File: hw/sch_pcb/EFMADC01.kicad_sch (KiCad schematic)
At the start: 36 parts, among them J1 3.3-5V, J2 HEADER_2x01, J4 HEADER_2x01_PARALLEL, J5 HEADER_2x01_PARALLEL, J6 HEADER_2x01_PARALLEL, J7 HEADER_2x01_PARALLEL, J9 MCX, M1 RFShield_TwoPieces, M2 HOLE, M3 HOLE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

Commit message: Rounted PCB Added silkscreen text.
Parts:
- removed C6: 1uF, Mlab_L:FIR_0805, symbol PCRD06A-rescue:EMI_Filter_C-Device
- removed C7: 100nF, Capacitor_SMD:C_0805_2012Metric, symbol ISM02A-rescue:C_Small-Device-ISM02A-rescue
- removed C9: 10uF, Capacitor_Tantalum_SMD:CP_EIA-3216-18_Kemet-A, symbol Device:C_Polarized
- removed D2: BZV55C-6,2V, Diode_SMD:D_MiniMELF, symbol ISM02A-rescue:D_ZENER-MLAB_D
- added C6, C7: 100nF, Capacitor_SMD:C_0805_2012Metric, symbol Device:C
- added C9: 10uF, Capacitor_SMD:C_0805_2012Metric, symbol Device:C
- added D2: BZV55C-6,2V, Diode_SMD:D_MiniMELF, symbol Device:D_Zener
- added R4, R5, R6, R7: 33R, Resistor_SMD:R_0805_2012Metric, symbol Device:R
- C1, C2, C3: footprint Capacitor_SMD:C_0603_1608Metric -> Capacitor_SMD:C_0805_2012Metric; UST_ID 5c70984812875079b91f8bf2 -> 6508260b462c6d9e720541f1
- C10, C12: UST_ID 5c70984812875079b91f8bf2 -> 5c70984712875079b91f8b4c
- C4: footprint Capacitor_SMD:C_0603_1608Metric -> Capacitor_SMD:C_0805_2012Metric; UST_ID 5c70984812875079b91f8bec -> 5c70984812875079b91f8ba6
- C5: footprint Capacitor_SMD:C_0603_1608Metric -> Capacitor_SMD:C_0805_2012Metric; UST_ID 5c70984812875079b91f8bf2 -> 5c70984712875079b91f8b4c
- D1: footprint Diode_SMD:D_SOD-523 -> Diode_SMD:D_SMB
- M1: UST_ID2 5c7275631287500b4e11302f -> (none)
- R1, R2, R3: footprint Resistor_SMD:R_0603_1608Metric -> Resistor_SMD:R_0805_2012Metric
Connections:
- net +3.3VA is gone; now on net VCC: C5.2, U1.1 (Vin), U2.5 (V+)
- net GND: now also C6.2, C9.2, D2.2 (A)
- net GNDA: now also C7.2
- net VCC: now also C8.1, J1.3, J1.4, C6.1, C7.1, C9.1, D2.1 (K)
- net at J4.1, J4.2: now also R4.2; no longer U4.8 (SCK)
- net at J7.1, J7.2: now also R7.2; no longer U4.1 (CONV)
- net at J5.1, J5.2: now also R5.2; no longer U4.7 (SDO)
- net at J6.1, J6.2: now also R6.2; no longer U4.6 (SDI)
- new net: R7.1, U4.1 (CONV)
- new net: R4.1, U4.8 (SCK)
- new net: R5.1, U4.7 (SDO)
- new net: R6.1, U4.6 (SDI)
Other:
- moved on the sheet: C1, D1, J4, J5, J6, J7, U1

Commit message: Cleanup net names in schematics.
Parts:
- U1: value ISL21080DIH312Z-TK 1V25 -> ISL21080CIH315ZT; UST_ID 5c70984712875079b91f8b7a -> 5c70984712875079b91f8b0a
- U3: UST_ID (none) -> 67d36d64ee7fc534862c3ebc
- U4: UST_ID (none) -> 651eae84462c6d9e7205573b
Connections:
- net REF_1V25 renamed REF
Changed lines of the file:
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@@
 		)
 	)
-	(label "REF_1V25"
+	(label "REF"
 		(at 91.44 106.68 180)
 		(effects
@@
 		)
 	)
-	(label "REF_1V25"
+	(label "REF"
 		(at 148.59 128.27 180)
 		(effects
@@
 		)
 	)
-	(label "REF_1V25"
+	(label "REF"
 		(at 109.22 160.02 180)
 		(effects
@@
 		)
 	)
-	(label "REF_1V25"
+	(label "REF"
 		(at 60.96 49.53 0)
 		(effects
@@
 			)
 		)
-		(property "Value" "ISL21080DIH312Z-TK  1V25"
+		(property "Value" "ISL21080CIH315ZT"
 			(at 41.91 40.64 90)
 			(effects
@@
 			)
 		)
-		(property "Description" "2.0V 25μA Micropower Voltage Reference, SOT-23"
+		(property "Description" "1.5V 25μA Micropower Voltage Reference, SOT-23"
 			(at 48.26 49.53 0)
 			(effects
@@
 			)
 		)
-		(property "UST_ID" "5c70984712875079b91f8b7a"
+		(property "UST_ID" "5c70984712875079b91f8b0a"
 			(at 48.26 49.53 0)
 			(effects
@@
 			)
 		)
-		(property "UST_ID" ""
+		(property "UST_ID" "67d36d64ee7fc534862c3ebc"
 			(at 157.48 71.12 0)
 			(effects
@@
 			(at 172.72 125.73 0)
 			(effects
+				(font
+					(size 1.27 1.27)
+				)
+				(hide yes)
+			)
+		)
+		(property "UST_ID" "651eae84462c6d9e7205573b"
+			(at 172.72 125.73 0)
+			(effects

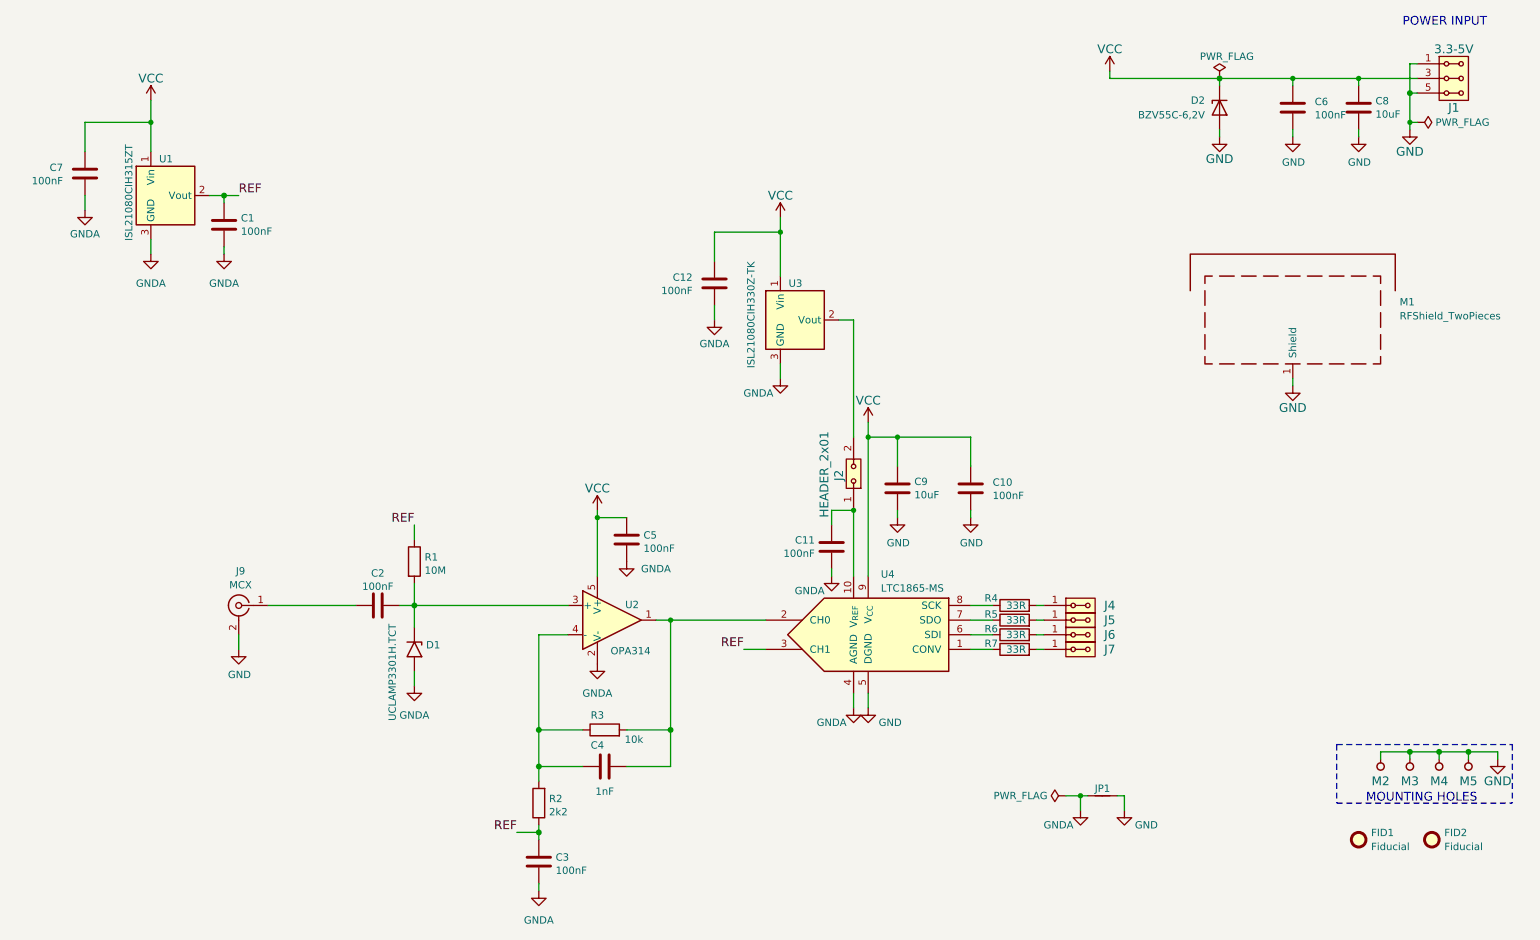
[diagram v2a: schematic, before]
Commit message: Implement buffer to reference voltage.
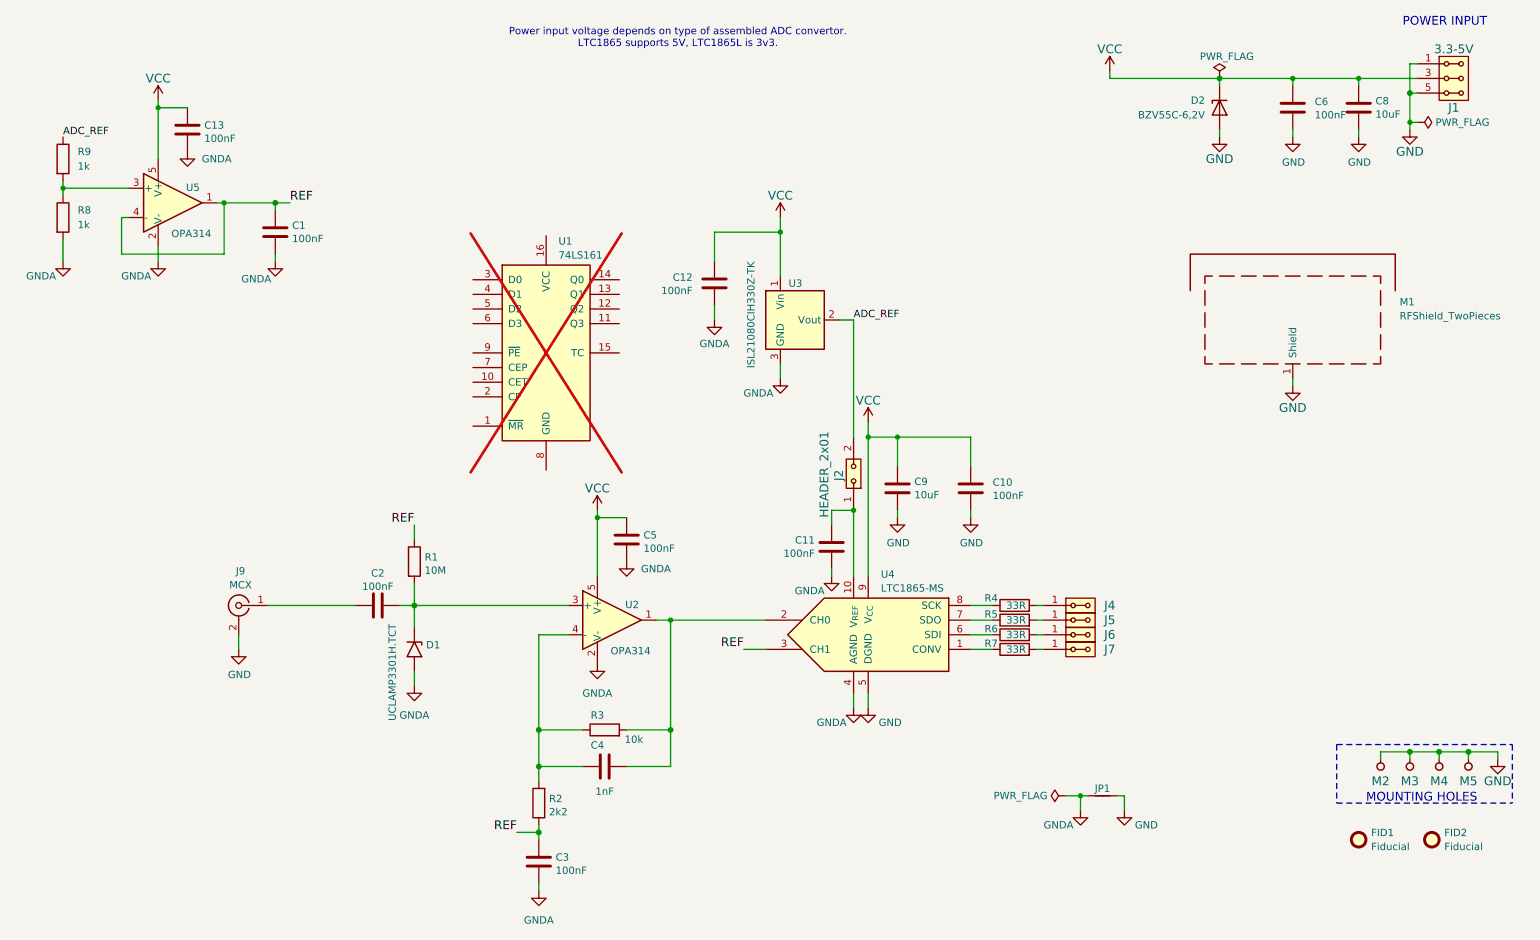
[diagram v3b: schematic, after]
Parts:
- removed C7: 100nF, Capacitor_SMD:C_0805_2012Metric, symbol Device:C
- removed U1: ISL21080CIH315ZT, Package_TO_SOT_SMD:SOT-23, symbol Reference_Voltage:ISL21070CIH320Z-TK
- added C13: 100nF, Capacitor_SMD:C_0805_2012Metric, symbol Device:C
- added R8, R9: 1k, Resistor_SMD:R_0805_2012Metric, symbol Device:R
- added U1: 74LS161, symbol 74xx:74LS161
- added U5: OPA314, Package_TO_SOT_SMD:SOT-23-5, symbol Amplifier_Operational:OPA330xxDBV
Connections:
- net GNDA: now also C13.1, R8.2, U5.2 (V-)
- net REF: now also U5.1, U5.4 (-)
- net VCC: now also C13.2, U5.5 (V+)
- net ADC_REF: now reaches J2.2, U3.2 (Vout)
- net ADC_REF: now also R9.1
- new net: R8.1, R9.2, U5.3 (+)
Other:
- note added: "Power input voltage depends on type of assembled ADC convertor. LTC1865 supports 5V, LTC1865L is 3v3."
- moved on the sheet: C1
